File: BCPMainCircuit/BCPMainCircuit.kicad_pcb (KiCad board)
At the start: 2 copper layers, 94 x 88 mm, 45 parts, among them Q1 IRLB8721PBF, SW1 Switch, U1 MCP9601T-E/MX, U2 Pico 2, U3 Logger, U4 GPS, U5 BNO055, U6 BME280, U7 MIC2940A-3.3WT, U8 MCP9601T-E/MX

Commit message: minor changes n stuff
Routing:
- net +3.3V: track 320.5 -> 311.3 mm, vias 2 -> 0
- net GND: vias 36 -> 41

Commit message: lsm6dso
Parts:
- added REF**: BAT_1079, Gabriel_footprints:BAT_1079, F.Cu at (33.0, 98.4)
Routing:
- net GND: vias 41 -> 51

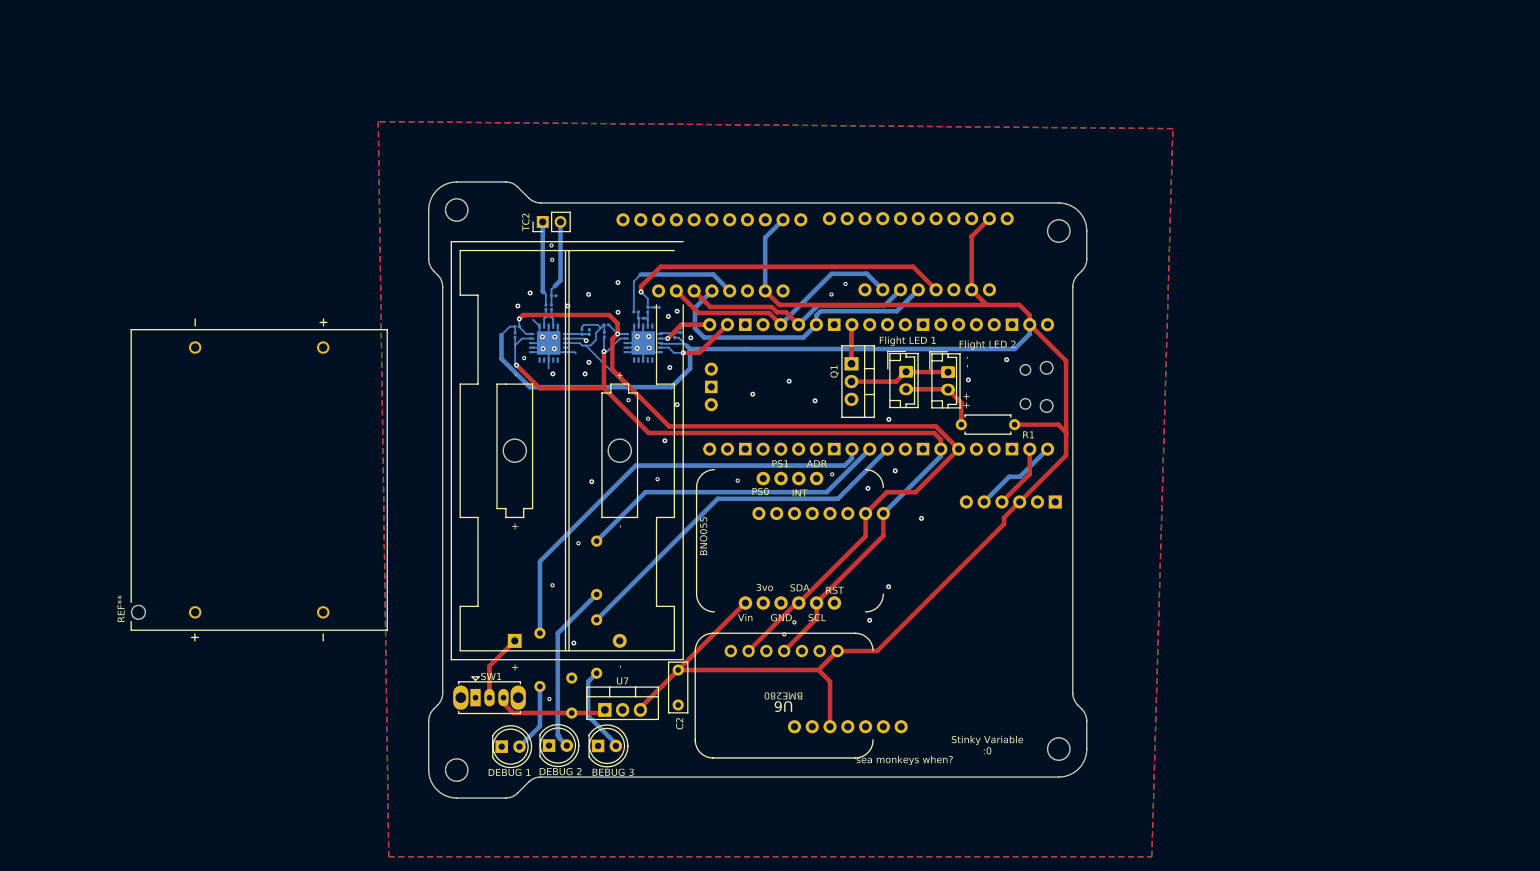
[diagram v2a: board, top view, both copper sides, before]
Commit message: minor changes (everything is being redone using smd components instead of breakout boards) still need : gps antenna + schematic (capacitors?) IMU (current one needs 1.8v!!!!!!!!!!!!!!!!) RGB LEDs? 16:2 mux? sd card needs reviewing (why are things laid out that way???)
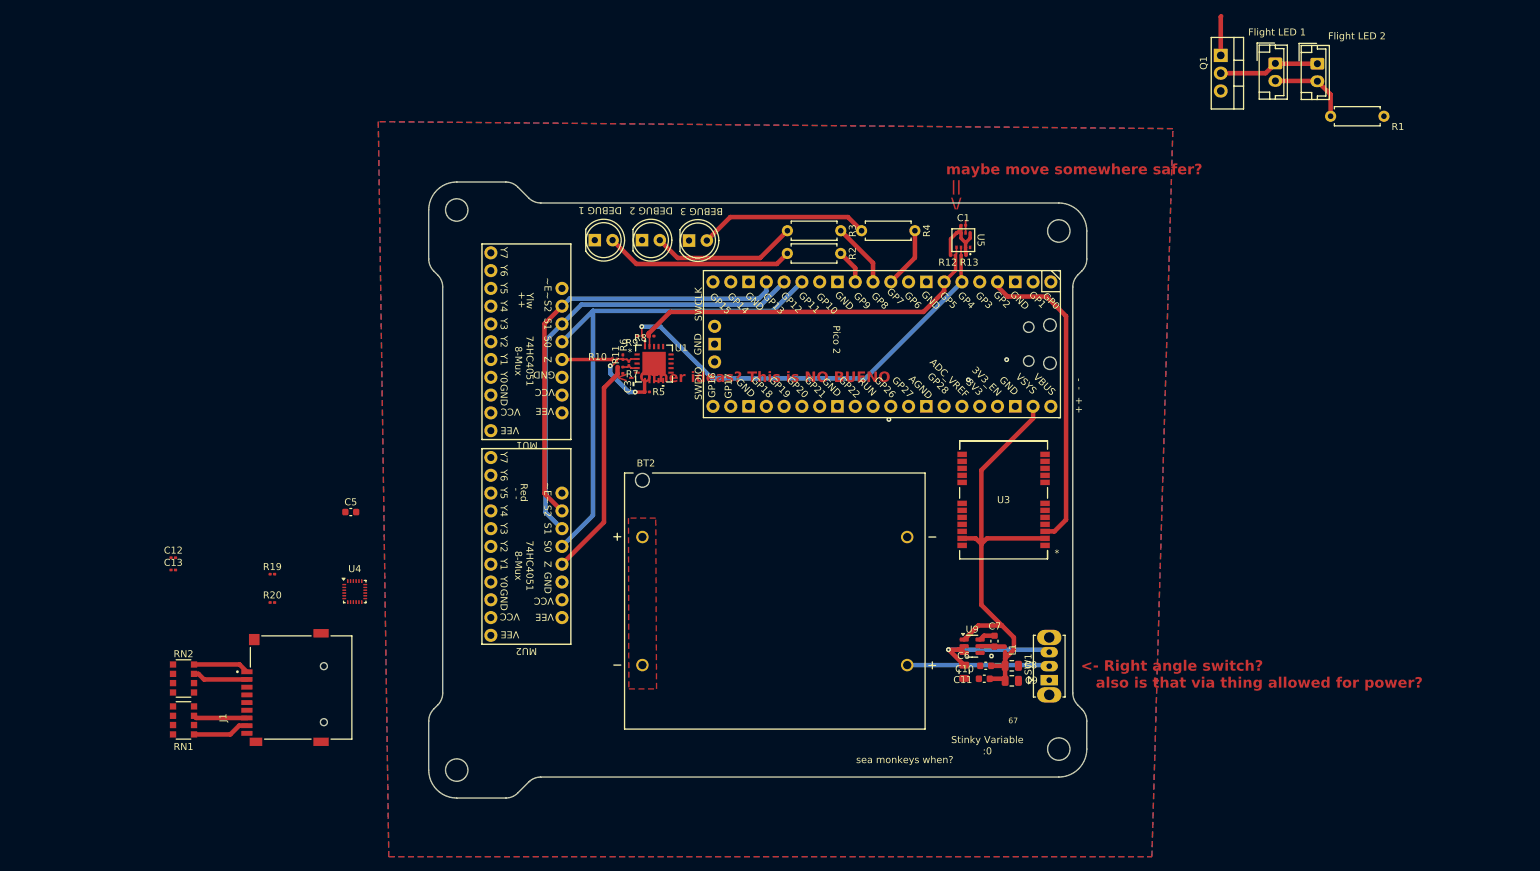
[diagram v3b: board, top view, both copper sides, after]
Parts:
- removed C2: 10u, Capacitor_THT:C_Disc_D7.0mm_W2.5mm_P5.00mm
- removed C4: 0u1f, Capacitor_SMD:C_0201_0603Metric
- removed R14: 100, Resistor_SMD:R_0201_0603Metric
- removed R15: 1M, Resistor_SMD:R_0201_0603Metric
- removed R16: 2M, Resistor_SMD:R_0201_0603Metric
- removed R17, R18: 10k, Resistor_SMD:R_0201_0603Metric
- removed the REF** at (33.0, 98.4)
- removed TC2: Thermocouple, Connector_PinHeader_2.54mm:PinHeader_1x02_P2.54mm_Vertical
- removed U6: BME280, Gabriel_footprints:BMP280
- removed U7: MIC2940A-3.3WT, Package_TO_SOT_THT:TO-220-3_Vertical
- removed U8: MCP9601T-E/MX, Gabriel_footprints:MQFN20_NU_MCH
- added C10: 4u7F, Capacitor_SMD:C_0603_1608Metric, F.Cu at (136.7, 125.0)
- added C11: 1uF, Capacitor_SMD:C_0603_1608Metric, F.Cu at (136.5, 126.8)
- added C12: 0u1f, Capacitor_SMD:C_0201_0603Metric, F.Cu at (20.7, 109.5)
- added C13: 0u1f, Capacitor_SMD:C_0201_0603Metric, F.Cu at (20.7, 111.3)
- added C5: 1uF, Capacitor_SMD:C_0603_1608Metric, F.Cu at (46.0, 103.0)
- added C6: 10uF, Capacitor_SMD:C_0805_2012Metric, F.Cu at (133.7, 125.8)
- added C7: 100nF, Capacitor_SMD:C_0603_1608Metric, F.Cu at (138.0, 121.4)
- added C8: 22uF, Capacitor_SMD:C_0805_2012Metric, F.Cu at (140.4, 125.0)
- added C9: 22uF, Capacitor_SMD:C_0805_2012Metric, F.Cu at (140.4, 127.1)
- added J1: MSD-4-A, Gabriel_footprints:CUI_MSD-4-A, F.Cu at (38.9, 128.1)
- added L1: 4u7H, Inductor_SMD:L_0201_0603Metric, F.Cu at (139.5, 122.6)
- added R19: 10kΩ, Resistor_SMD:R_0201_0603Metric, F.Cu at (34.8, 111.9)
- added R20: 10kΩ, Resistor_SMD:R_0201_0603Metric, F.Cu at (34.8, 115.9)
- added RN1: CAY16-4702F4LF, Resistor_SMD:R_Array_Convex_4x1206, F.Cu at (22.1, 132.8)
- added RN2: CAY16-4702F4LF, Resistor_SMD:R_Array_Convex_4x1206, F.Cu at (22.1, 126.8)
- added U9: AP63203WU-7, Package_TO_SOT_SMD:TSOT-23-6, F.Cu at (134.8, 122.2)
- BT2: footprint Battery:BatteryHolder_Keystone_2462_2xAA -> Gabriel_footprints:BAT_1079
- C1: value 10u -> 200nf; footprint Capacitor_THT:C_Disc_D7.0mm_W2.5mm_P5.00mm -> Capacitor_SMD:C_0201_0603Metric; moved to F.Cu
- C3, MU1, MU2, R10, R11, R5, R6, R7, R8, R9, U1, U2: moved to F.Cu
- R1: value ???R -> 20Ω
- R12: value 2M -> 4.7kΩ; moved to F.Cu
- R13: value 100 -> 4.7kΩ; moved to F.Cu
- R2, R3, R4: value ???R -> 65Ω; moved to F.Cu
- U3: value Logger -> NEO-M9N-00B; footprint Trantor:MODULE_DEV-13712 -> Gabriel_footprints:NEO-M9N; moved to F.Cu
- U4: value GPS -> ICM-20948; footprint Gabriel_footprints:NEO-M9N GPS -> Sensor_Motion:InvenSense_QFN-24_3x3mm_P0.4mm; moved to F.Cu
- U5: value BNO055 -> BME280; footprint Trantor:BNO055 -> Gabriel_footprints:BME280(1)
- moved C1 89.3 mm to (133.5, 62.0), turned to 0 degrees
- moved SW1 82.0 mm to (145.8, 127.0), turned to 90 degrees
- moved R4 73.7 mm to (119.0, 62.8), turned to 0 degrees
- moved D2 73.6 mm to (80.9, 64.2)
- moved D3 73.4 mm to (87.6, 64.2)
- moved D4 73.4 mm to (94.3, 64.2)
- moved MU2 72.6 mm to (71.1, 109.9), turned to 180 degrees
- moved R2 71.2 mm to (108.4, 66.0), turned to 0 degrees
- moved Q1 68.7 mm to (170.3, 37.8)
- moved D1 68.7 mm to (178.1, 38.9)
- moved D5 68.7 mm to (184.1, 39.0)
- moved R1 68.7 mm to (193.6, 46.5)
- moved U4 63.9 mm to (46.6, 114.3)
- moved R13 59.3 mm to (133.6, 66.3), turned to 0 degrees
- moved R3 58.7 mm to (108.4, 62.8), turned to 0 degrees
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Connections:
- C1 pad 1: Net-(SW1-A) -> +3.3V
- C3 pad 1: Net-(U1-VIN+) -> /VSense1
- R10 pad 2: Net-(U1-VIN+) -> /VSense1
- R12 pad 1: /TC-2 -> +3.3V
- R12 pad 2: GND -> /SCL
- R13 pad 1: /TC-2 -> /SDA
- R13 pad 2: Net-(U8-VIN-) -> +3.3V
- SW1 pad 3: Net-(SW1-A) -> BATT+
- U1 pad 2: Net-(U1-VIN+) -> /VSense1
- U2 pad 15: unconnected-(U2-GPIO11-Pad15) -> /TC-Sel1
- U2 pad 16: unconnected-(U2-GPIO12-Pad16) -> /TC-Sel2
- U2 pad 17: unconnected-(U2-GPIO13-Pad17) -> /TC-Sel3
- U2 pad 19: unconnected-(U2-GPIO14-Pad19) -> /ThermoOCwarn
- U2 pad 20: unconnected-(U2-GPIO15-Pad20) -> /ThermoSCwarn
- U2 pad 21: /ThermoSCwarn -> SD_MISO
- U2 pad 22: /ThermoOCwarn -> SD_CS
- U2 pad 24: unconnected-(U2-GPIO18-Pad24) -> SD_SCK
- U2 pad 25: /TC-Sel3 -> SD_MOSI
- U2 pad 26: /TC-Sel2 -> unconnected-(U2-GPIO20-Pad26)
- U2 pad 27: /TC-Sel1 -> SD_CD
- U2 pad 4: unconnected-(U2-GPIO2-Pad4) -> /TimePulseGPS
- U3 pad 1: GND -> unconnected-(U3-SAFEBOOT_N-Pad1)
- U3 pad 2: GND -> +3.3V
- U3 pad 3: +3.3V -> /TimePulseGPS
- U3 pad 4: /MCURX -> unconnected-(U3-EXTINT-Pad4)
- U3 pad 5: /MCUTX -> unconnected-(U3-USB_DM-Pad5)
- U4 pad 11: +3.3V -> unconnected-(U4-FSYNC-Pad11)
- U4 pad 5: GND -> unconnected-(U4-NC-Pad5)
- U4 pad 7: /SDA -> unconnected-(U4-AUX_CL-Pad7)
- U4 pad 8: /SCL -> +1.8V
- U4 pad 9: GND -> unconnected-(U4-SDO/AD0-Pad9)
- U5 pad 1: +3.3V -> GND
- U5 pad 2: unconnected-(U5-3V0-Pad2) -> +3.3V
- U5 pad 3: GND -> /SDA
- U5 pad 4: /SDA -> /SCL
- U5 pad 5: /SCL -> +3.3V
- U5 pad 6: unconnected-(U5-RST-Pad6) -> +3.3V
- U5 pad 7: unconnected-(U5-PS0-Pad7) -> GND
- U5 pad 8: unconnected-(U5-PS1-Pad8) -> +3.3V
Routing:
- net +3.3V: track 311.3 -> 79.1 mm
- net /SCL: track 122.6 -> 53.6 mm, vias 2 -> 0
- net /SDA: track 126.0 -> 62.5 mm, vias 2 -> 1
- net /DEBUG1: track 62.2 -> 4.92 mm
- net /TimePulseGPS: track 0.00 -> 45.0 mm
- net /DEBUG3: track 51.7 -> 8.73 mm
- net GND: track 41.3 -> 1.78 mm, vias 51 -> 4
- net /DEBUG2: track 44.5 -> 9.22 mm
- net /TC-Sel2: track 33.5 -> 65.4 mm
- net /TC-Sel1: track 42.4 -> 73.4 mm
- net /TC-Sel3: track 35.4 -> 62.7 mm
- net BATT+: track 0.00 -> 21.2 mm, vias 0 -> 1
- net /TC-RED: track 49.0 -> 31.4 mm, vias 1 -> 0
- net Net-(D2-A): track 9.79 -> 27.0 mm
- net Net-(SW1-A): track 16.0 -> 0.00 mm
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- added copper zone on F.Cu, net BatTerms
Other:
- board text added: "67"
- board text added: "<- Other ideas? This is NO BUENO"
- board text added: "<- Right angle switch? also is that via thing allowed for power?"
- board text added: "maybe move somewhere safer? || \/"
- board text removed: "BLK"
- board text removed: "GND"
- board text removed: "GPS"
- board text removed: "GRN"
- board text removed: "RX"
- board text removed: "TX"
- board text removed: "Vin"

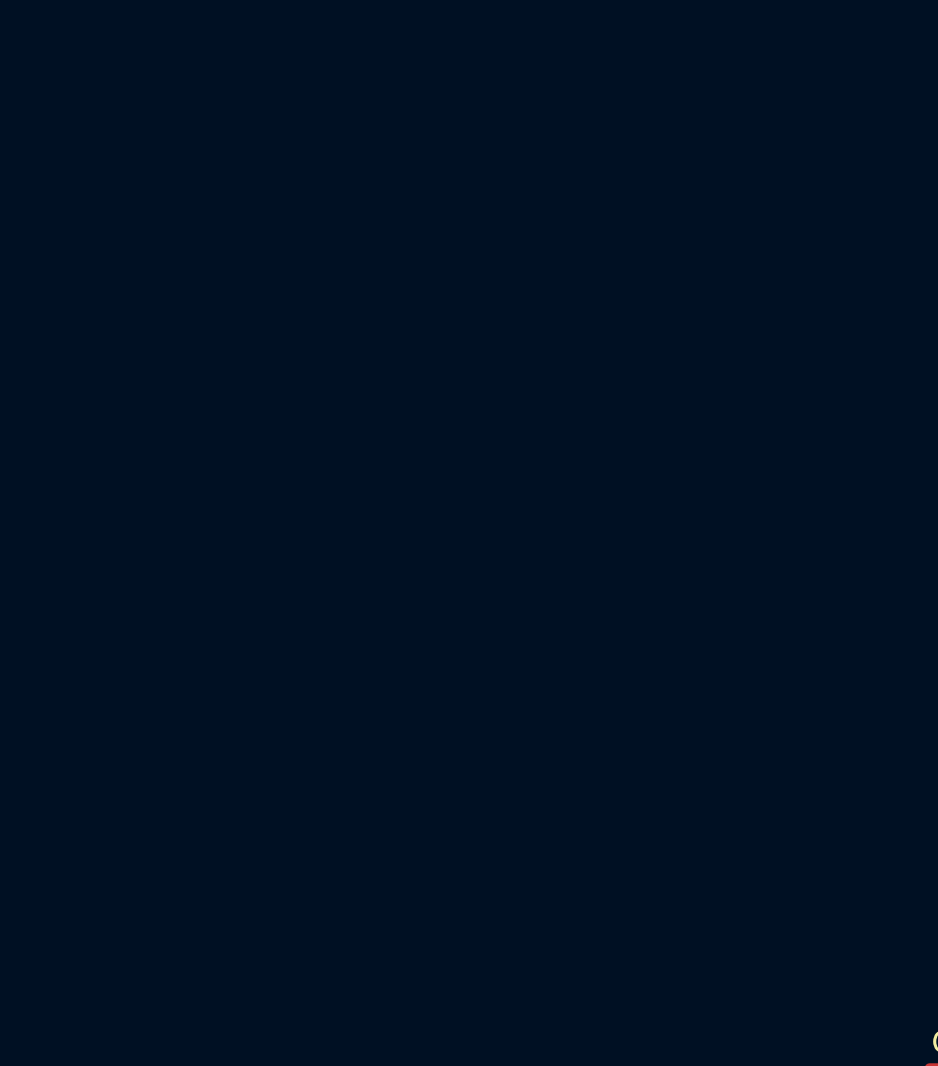
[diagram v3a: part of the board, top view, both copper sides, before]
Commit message: in the middle of stuff NOTES: replace 2xmux with 1x cheaper mux? RGB leds HOW? how to sd card? magnetometer trade check stock of resistors, capacitors, inductors, sd slots, etc etc
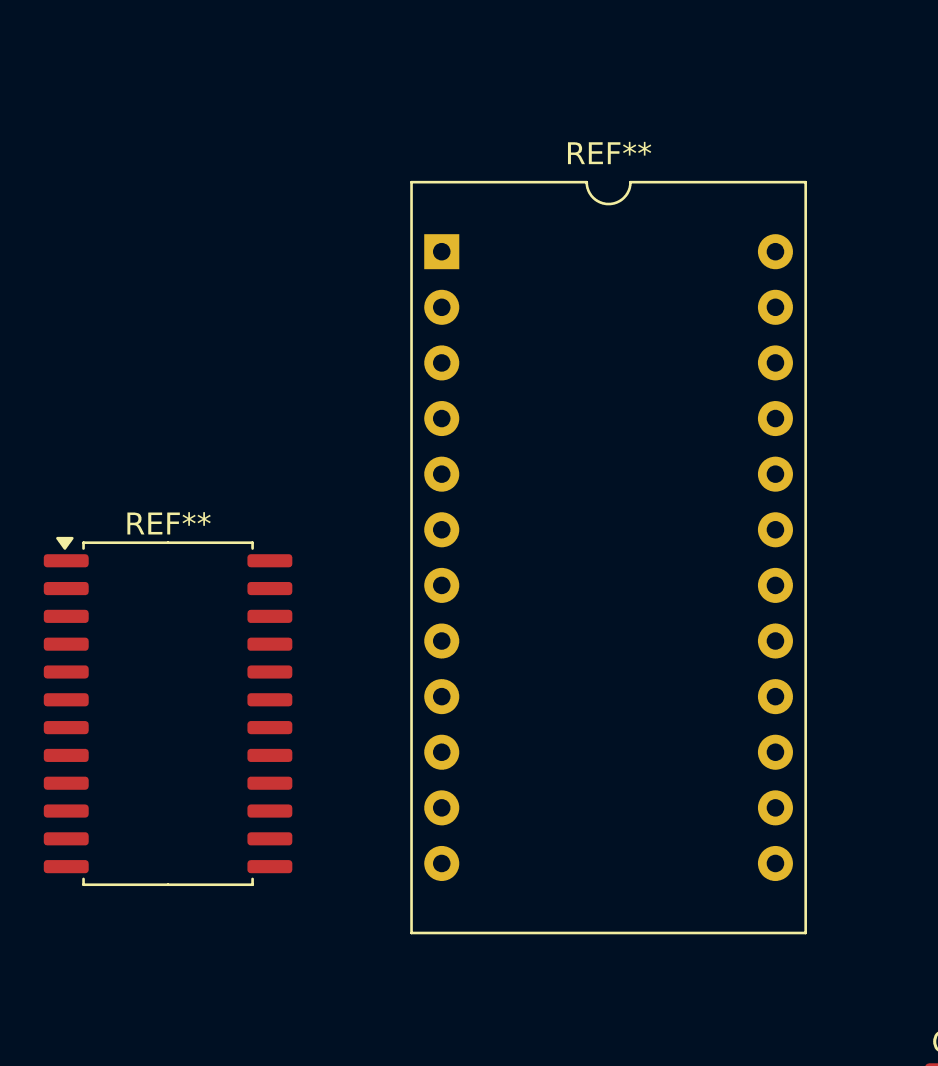
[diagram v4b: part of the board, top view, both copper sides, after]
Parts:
- added REF**: DIP-24_18.0mmx34.29mm_W15.24mm, Package_DIP:DIP-24_18.0mmx34.29mm_W15.24mm, F.Cu at (22.8, 65.5)
- added REF**: SOIC-24W_7.5x15.4mm_P1.27mm, Package_SO:SOIC-24W_7.5x15.4mm_P1.27mm, F.Cu at (10.2, 86.5)
